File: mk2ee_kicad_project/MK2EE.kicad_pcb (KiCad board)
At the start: 2 copper layers, 209.5 x 132.1 mm, 81 parts, among them J1 L712RA, J10 Conn_01x02_Male, J11 Conn_02x6_Male, J12 Conn_01x06_Male, J13 Conn_01x06_Male, J2 Conn_02x6_Male, J3 Conn_01x02_Male, J4 Conn_02x03_Male, J5 Conn_02x03_Male, J6 Conn_01x04_Male, J7 Conn_01x04_Male, J8 Conn_02x03_Male, J9 Conn_02x03_Male, U1 NUCLEO-F411RE, U10 AS5047D-ATSM, U11 74HC595, U2 TSR_1-24150, U3 NCP718xSN330, U4 TSR_1-2465, U5 NCP718xSN330, U6 74HC595, U7 DRV8818PWP, U8 AS5047D-ATSM, U9 74HC595

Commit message: PCB designs are updated
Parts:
- added H5: MountingHole_3.2mm_M3, MountingHole:MountingHole_3.2mm_M3, F.Cu at (136.3, 148.4)
- added H5: MountingHole_3.2mm_M3, MountingHole:MountingHole_3.2mm_M3, F.Cu at (167.3, 179.4)
- C10, C11, C12, C13, C6, C7, C9, J7, R1, R6, R7, R8, U4, U7: moved to B.Cu
- R2, R3, R4, R5: footprint Resistor_SMD:R_0805_2012Metric_Pad1.15x1.40mm_HandSolder -> Resistor_SMD:R_1206_3216Metric; moved to B.Cu
- moved C6 224.8 mm to (246.9, 116.6), turned to 270 degrees
- moved C7 214.1 mm to (246.0, 132.7), turned to 90 degrees
- moved R1 199.5 mm to (249.4, 116.6), turned to 270 degrees
- moved R6 181.8 mm to (248.4, 132.7), turned to 90 degrees
- moved C13 179.4 mm to (247.5, 127.7)
- moved R3 176.1 mm to (247.5, 125.4), turned to 180 degrees
- moved R2 170.4 mm to (247.5, 123.0)
- moved U7 169.9 mm to (229.1, 127.9), turned to 180 degrees
- moved R5 166.8 mm to (246.7, 138.5), turned to 180 degrees
- moved R8 164.8 mm to (237.7, 136.7)
- moved R4 161.6 mm to (246.6, 140.9)
- moved R7 153.8 mm to (238.4, 116.2), turned to 90 degrees
- moved C10 153.7 mm to (213.9, 134.7), turned to 180 degrees
- moved C9 152.4 mm to (217.3, 125.2), turned to 90 degrees
- moved U6 151.7 mm to (229.2, 140.1), turned to 270 degrees
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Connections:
- R2 pad 2: VCC2 -> VCCB3v3
- R4 pad 2: VCC2 -> VCCB3v3
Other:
- board size 209.5 x 132.1 mm -> 163.6 x 169.7 mm

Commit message: all components are connected
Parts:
- added REF**: MountingHole_3.2mm_M3, MountingHole:MountingHole_3.2mm_M3, F.Cu at (163.1, 68.9)
- added REF**: MountingHole_3.2mm_M3, MountingHole:MountingHole_3.2mm_M3, F.Cu at (163.1, 47.9)
- C11: moved to F.Cu
- C19, C8, J10, J8, J9: moved to B.Cu
- J11, J2: footprint Connector_PinSocket_2.54mm:PinSocket_2x06_P2.54mm_Horizontal -> Connector_IDC:IDC-Header_2x06_P2.54mm_Horizontal
- TP1, TP2, TP3, TP4, TP5, TP7, TP8, TP9: footprint TestPoint:TestPoint_Pad_D4.0mm -> TestPoint:TestPoint_Pad_D1.5mm
- moved LED2 94.7 mm to (149.2, 89.7)
- moved C6 91.4 mm to (162.5, 151.6), turned to 0 degrees
- moved R7 90.1 mm to (153.6, 146.6), turned to 180 degrees
- moved C13 89.7 mm to (160.3, 148.6)
- moved R3 89.7 mm to (160.3, 146.3)
- moved R2 89.6 mm to (160.3, 143.9)
- moved R1 89.2 mm to (167.4, 151.6), turned to 180 degrees
- moved C7 86.6 mm to (162.5, 155.2), turned to 0 degrees
- moved R14 86.1 mm to (153.0, 85.4), turned to 270 degrees
- moved R8 84.2 mm to (156.9, 160.3), turned to 270 degrees
- moved R6 84.1 mm to (167.4, 155.2), turned to 180 degrees
- moved C9 82.8 mm to (140.3, 155.6), turned to 180 degrees
- moved U6 82.3 mm to (151.1, 166.2)
- moved U7 82.3 mm to (151.1, 154.0)
- moved R12 79.5 mm to (149.3, 85.4), turned to 90 degrees
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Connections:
- J11 pad 10: SerialDataDr4 -> SerialDataInEn4
- J11 pad 11: PO-CLKDr4 -> CLKEn4
- J11 pad 12: SH-CLKDr4 -> PO-CLKDr4
- J11 pad 2: GND -> VCCF3v3
- J11 pad 3: VCCF3v3 -> GND
- J11 pad 4: PWM4 -> SH-CLKEn4
- J11 pad 5: CLKEn4 -> SerialDataDr4
- J11 pad 6: MISO4 -> PO-CLKEn4
- J11 pad 7: SerialDataInEn4 -> SH-CLKDr4
- J11 pad 8: PO-CLKEn4 -> MISO4
- J11 pad 9: SH-CLKEn4 -> PWM4
- J12 pad 1: PO-CLKEn4 -> VMC
- J12 pad 2: SerialDataOutEn4 -> GND
- J12 pad 3: CLKEn4 -> Net-(J12-Pad3)
- J12 pad 4: MISO4 -> SerialDataDr4
- J12 pad 5: SH-CLKEn4 -> MISO4
- J12 pad 6: Net-(J12-Pad6) -> CLKEn4
- J13 pad 1: GND -> PO-CLKEn4
- J13 pad 2: VMC -> SH-CLKEn4
- J13 pad 3: SerialDataDr4 -> SerialDataOutEn4
- J13 pad 4: PO-CLKDr4 -> SH-CLKDr4
- J13 pad 5: SH-CLKDr4 -> PWM4
- J13 pad 6: PWM4 -> PO-CLKDr4
- J2 pad 1: VMA -> CLK1
- J2 pad 10: SerialDataOutDr1 -> SH-CLKEn1
- J2 pad 11: PO-CLKDr1 -> VMA
- J2 pad 12: SH-CLKDr1 -> VCCA3v3
- J2 pad 2: GND -> PO-CLKDr1
- J2 pad 3: VCCA3v3 -> PWM1
- J2 pad 4: PWM1 -> SerialDataOutEn1
- J2 pad 5: MOSI1 -> SH-CLKDr1
- J2 pad 7: SerialDataOutEn1 -> SerialDataOutDr1
- J2 pad 9: SH-CLKEn1 -> GND
- J4 pad 1: VMB -> SerialDataInDr2
- J4 pad 2: GND -> VMB
- J4 pad 4: SerialDataInDr2 -> PWM2
- J4 pad 5: PWM2 -> SH-CLKDr2
- J4 pad 6: SH-CLKDr2 -> GND
- J5 pad 1: VMB -> SH-CLKDr2
- J5 pad 4: SerialDataOutDr2 -> PWM2
- J5 pad 5: PWM2 -> SerialDataOutDr2
- J5 pad 6: SH-CLKDr2 -> VMB
- J6 pad 2: GND -> PWM2
- J6 pad 3: PWM2 -> VCC6v5
- J6 pad 4: VCC6v5 -> GND
- J8 pad 1: PO-CLKEn3 -> SerialDataInEn3
- J8 pad 2: SerialDataInEn3 -> Net-(J8-Pad2)
- J8 pad 3: CLKEn3 -> PO-CLKEn3
- J8 pad 4: MISO3 -> CLKEn3
- J8 pad 6: Net-(J8-Pad6) -> MISO3
- J9 pad 1: PO-CLKEn3 -> SH-CLKEn3
- J9 pad 2: SerialDataOutEn3 -> MISO3
- J9 pad 3: CLKEn3 -> PO-CLKEn3
- J9 pad 4: MISO3 -> CLKEn3
- J9 pad 5: SH-CLKEn3 -> SerialDataOutEn3
- U1 pad CN10_16: Net-(U1-PadCN10_16) -> PO-CLKEn1
- U1 pad CN10_24: PO-CLKEn1 -> Net-(U1-PadCN10_24)
- U1 pad CN10_30: Net-(U1-PadCN10_30) -> SH-CLKEn1
- U1 pad CN10_33: MOSI1 -> Net-(U1-PadCN10_33)
- U1 pad CN7_34: SH-CLKEn1 -> CLK1
- U6 pad 1: USM0 -> USM1
- U6 pad 2: USM1 -> USM0
- U6 pad 3: STEP -> SRn
- U6 pad 4: SRn -> RESETn
- U6 pad 5: RESETn -> STEP
- U9 pad 15: CSn3 -> Net-(U9-Pad15)
- U9 pad 4: LED2-R3 -> LED2-B3
- U9 pad 6: LED2-B3 -> LED2-R3
- U9 pad 7: Net-(U9-Pad7) -> CSn3
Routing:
- net VMB: track 0.00 -> 175.0 mm, vias 0 -> 4
- net VMA: track 0.00 -> 133.7 mm
- net GND: track 0.00 -> 118.1 mm, vias 0 -> 16
- net PWM2: track 0.00 -> 103.1 mm
- net MISO3: track 0.00 -> 91.0 mm, vias 0 -> 1
- net CLKEn3: track 0.00 -> 83.8 mm, vias 0 -> 1
- net PO-CLKEn3: track 0.00 -> 61.0 mm
- net SH-CLKEn3: track 0.00 -> 59.0 mm
- net VCCA3v3: track 0.00 -> 55.6 mm
- net VCCA5V: track 0.00 -> 55.4 mm
- net MISO4: track 0.00 -> 55.2 mm
- net PO-CLKEn4: track 0.00 -> 55.1 mm, vias 0 -> 1
- net PWM4: track 0.00 -> 54.9 mm
- net CLKEn4: track 0.00 -> 53.8 mm, vias 0 -> 1
- net MISO1: track 0.00 -> 51.0 mm
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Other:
- board size 163.6 x 169.7 mm -> 173.3 x 172.9 mm

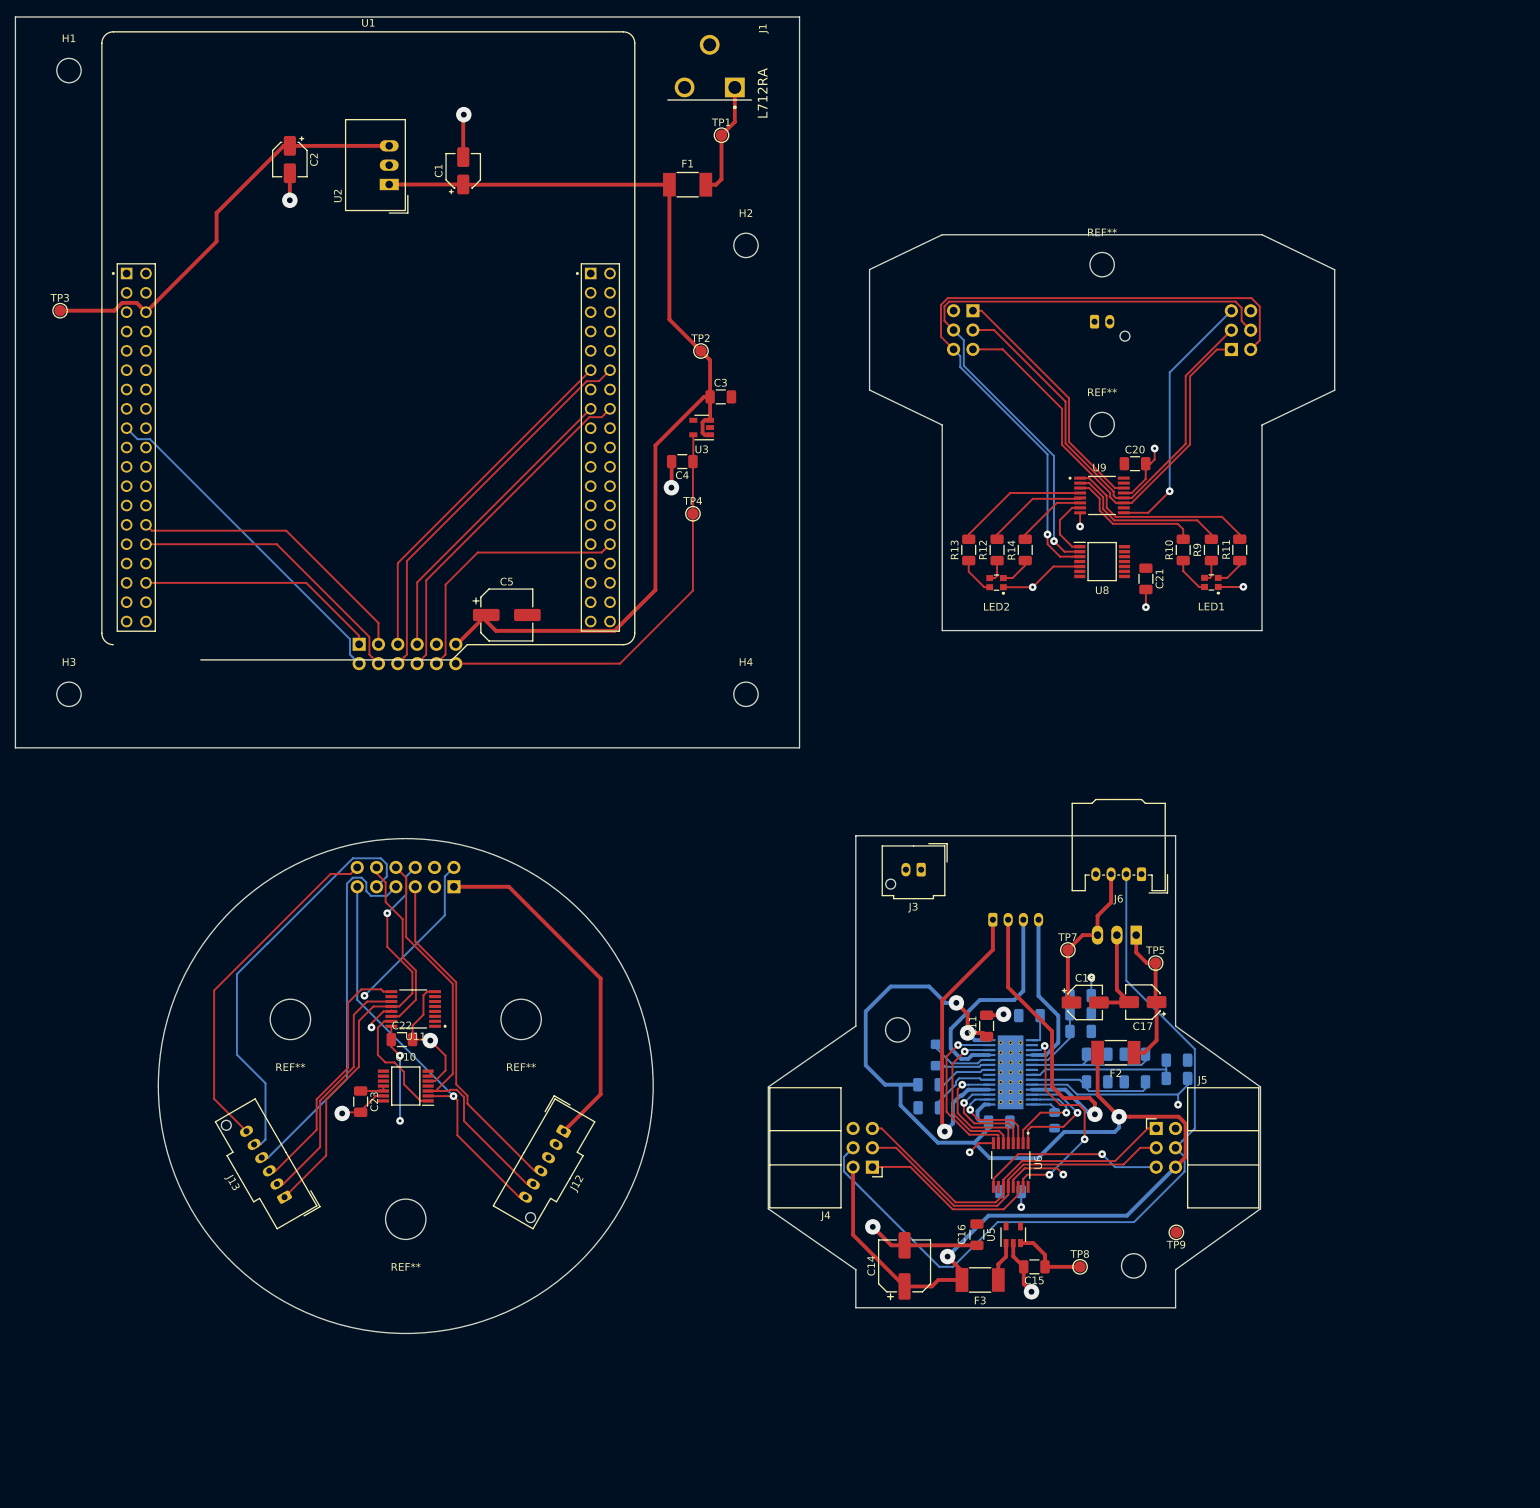
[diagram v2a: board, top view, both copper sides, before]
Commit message: New 3D model of Base part and PCB design is fixed
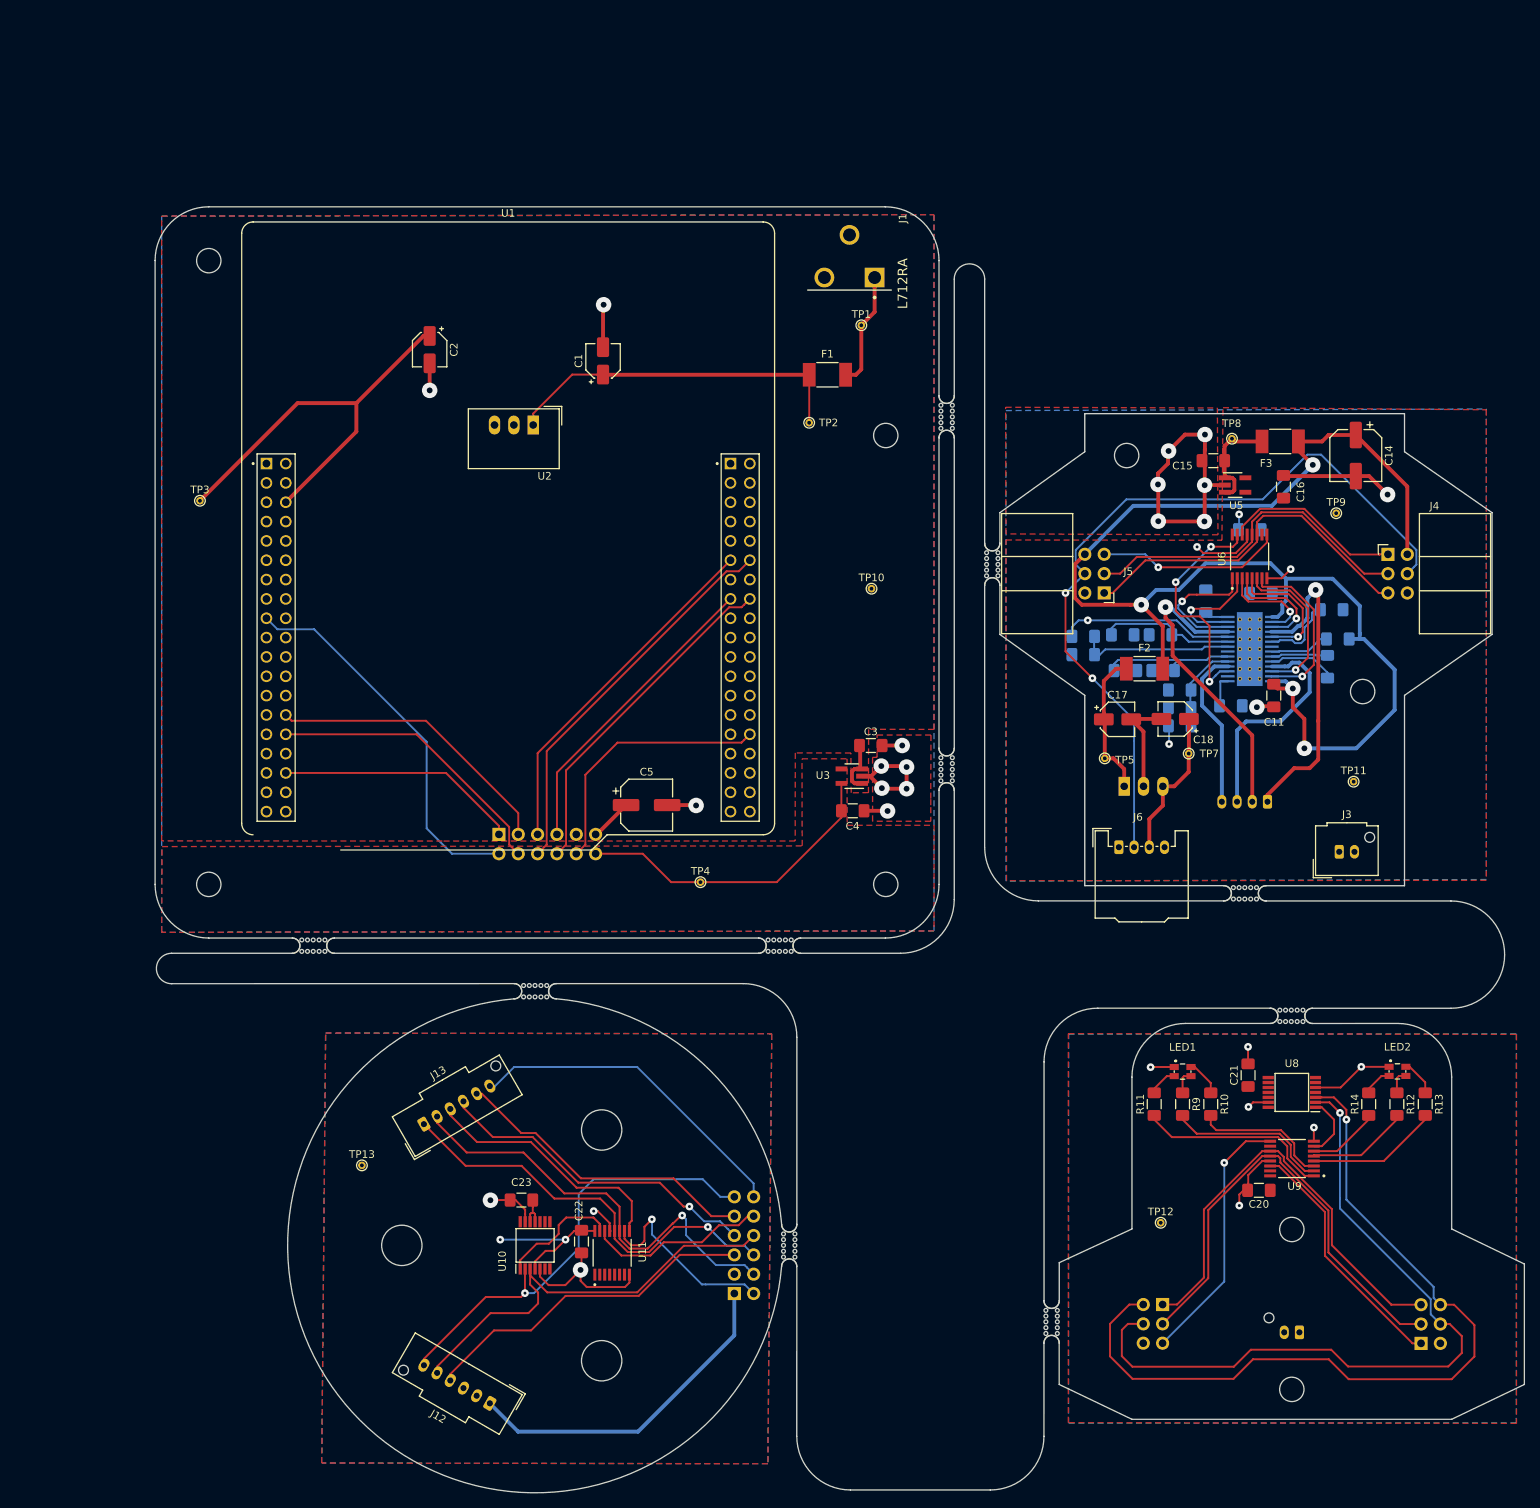
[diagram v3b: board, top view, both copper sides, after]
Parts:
- removed the H5 at (136.3, 148.4)
- removed the H5 at (167.3, 179.4)
- removed the REF** at (163.1, 68.9)
- removed the REF** at (163.1, 47.9)
- added H5: MountingHole_3.2mm_M3, MountingHole:MountingHole_3.2mm_M3, F.Cu at (197.3, 104.0)
- added H5: MountingHole_3.2mm_M3, MountingHole:MountingHole_3.2mm_M3, F.Cu at (166.3, 73.0)
- added REF**: MountingHole_3.2mm_M3, MountingHole:MountingHole_3.2mm_M3, F.Cu at (188.0, 174.6)
- added REF**: MountingHole_3.2mm_M3, MountingHole:MountingHole_3.2mm_M3, F.Cu at (188.0, 195.6)
- added TP10: GND, TestPoint:TestPoint_THTPad_D1.0mm_Drill0.5mm, F.Cu at (132.8, 90.5)
- added TP11: TestPoint, TestPoint:TestPoint_THTPad_D1.0mm_Drill0.5mm, F.Cu at (196.2, 115.8)
- added TP12: TestPoint, TestPoint:TestPoint_THTPad_D1.0mm_Drill0.5mm, F.Cu at (170.8, 173.8)
- added TP13: TestPoint, TestPoint:TestPoint_THTPad_D1.0mm_Drill0.5mm, F.Cu at (65.9, 166.2)
- added mouse-bite-3mm-slot: VAL**, MK2Library:mouse-bite-3mm-slot, F.Cu at (148.7, 87.3)
- added mouse-bite-3mm-slot: VAL**, MK2Library:mouse-bite-3mm-slot, F.Cu at (88.6, 143.3)
- added mouse-bite-3mm-slot: VAL**, MK2Library:mouse-bite-3mm-slot, F.Cu at (142.7, 67.9)
- added mouse-bite-3mm-slot: VAL**, MK2Library:mouse-bite-3mm-slot, F.Cu at (142.7, 114.2)
- added mouse-bite-3mm-slot: VAL**, MK2Library:mouse-bite-3mm-slot, F.Cu at (181.9, 130.5)
- added mouse-bite-3mm-slot: VAL**, MK2Library:mouse-bite-3mm-slot, F.Cu at (188.0, 146.6)
- added mouse-bite-3mm-slot: VAL**, MK2Library:mouse-bite-3mm-slot, F.Cu at (156.5, 186.8)
- added mouse-bite-3mm-slot: VAL**, MK2Library:mouse-bite-3mm-slot, F.Cu at (120.8, 137.4)
- added mouse-bite-3mm-slot: VAL**, MK2Library:mouse-bite-3mm-slot, F.Cu at (59.5, 137.4)
- added mouse-bite-3mm-slot: VAL**, MK2Library:mouse-bite-3mm-slot, F.Cu at (122.0, 176.7)
- C10, C11, C12, C13, C15, C16, C19, C20, C21, C22, C23, C3, C4, C6, C7, C8, C9: footprint Capacitor_SMD:C_1206_3216Metric -> Capacitor_SMD:C_1206_3216Metric_Pad1.42x1.75mm_HandSolder
- R1, R10, R11, R12, R13, R14, R2, R3, R4, R5, R6, R7, R9: footprint Resistor_SMD:R_1206_3216Metric -> Resistor_SMD:R_1206_3216Metric_Pad1.42x1.75mm_HandSolder
- R8: footprint Resistor_SMD:R_0805_2012Metric_Pad1.15x1.40mm_HandSolder -> Resistor_SMD:R_1206_3216Metric_Pad1.42x1.75mm_HandSolder
- TP1, TP2, TP3, TP4, TP5, TP7, TP8, TP9: footprint TestPoint:TestPoint_Pad_D1.5mm -> TestPoint:TestPoint_THTPad_D1.0mm_Drill0.5mm
- U3, U5: footprint Package_TO_SOT_SMD:SOT-23-5 -> Package_TO_SOT_SMD:SOT-23-5_HandSoldering
- moved J8 147.9 mm to (205.0, 189.6), turned to 0 degrees
- moved J10 135.5 mm to (189.0, 188.2), turned to 180 degrees
- moved J9 125.8 mm to (171.1, 184.5), turned to 180 degrees
- moved C14 121.8 mm to (196.4, 73.0), turned to 270 degrees
- moved F3 117.0 mm to (186.5, 71.1), turned to 180 degrees
- moved TP8 110.6 mm to (180.2, 70.8), turned to 180 degrees
- moved C15 108.5 mm to (177.7, 73.7)
- moved C16 106.2 mm to (186.9, 77.1), turned to 90 degrees
- moved J4 105.2 mm to (200.7, 86.0), turned to 0 degrees
- moved U5 102.7 mm to (180.6, 76.9), turned to 0 degrees
- moved C20 96.8 mm to (183.7, 169.5), turned to 180 degrees
- moved TP9 96.8 mm to (193.9, 80.6), turned to 0 degrees
- moved R13 94.3 mm to (205.6, 158.2), turned to 270 degrees
- moved C19 92.4 mm to (182.5, 82.7), turned to 0 degrees
- moved U9 90.6 mm to (188.1, 165.3), turned to 180 degrees
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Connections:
- C1 pad 1: VMA -> /supply/pwr2
- C3 pad 1: VMA -> VCCA5V
- C5 pad 1: VMA -> VCCA5V
- F1 pad P$2: VMA -> /supply/pwr2
- J2 pad 11: VMA -> VCCA5V
- TP2 pad 1: VMA -> /supply/pwr2
- U2 pad 1: VMA -> /supply/pwr2
- U3 pad 1: VMA -> VCCA5V
- U3 pad 3: VMA -> VCCA5V
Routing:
- net VMA: track 133.7 -> 0.00 mm
- net GND: track 118.1 -> 172.9 mm, vias 16 -> 28
- net /supply/pwr2: track 0.00 -> 46.2 mm
- net SH-CLKEn4: track 32.5 -> 57.9 mm, vias 0 -> 1
- net MISO3: track 91.0 -> 107.5 mm
- net PWM4: track 54.9 -> 40.5 mm
- net VCCA3v3: track 55.6 -> 41.8 mm
- net CLKEn3: track 83.8 -> 97.3 mm
- net VCCA5V: track 55.4 -> 68.8 mm
- net VCCF3v3: track 38.3 -> 49.6 mm
- net CLKEn4: track 53.8 -> 59.9 mm
- net SH-CLKDr4: track 50.0 -> 44.2 mm, vias 0 -> 1
- net PO-CLKDr1: track 44.5 -> 50.0 mm
- net /driver-1/2A: track 41.9 -> 39.9 mm
- net VMB: track 175.0 -> 177.0 mm
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- added copper zone on B.Cu, net GND
- added copper zone on F.Cu, net GND
- added copper zone on F.Cu, net VCCA3v3
- added copper zone on F.Cu, net VCCA5V
- added copper zone on F.Cu, net VCCB3v3
- added copper zone on F.Cu, net VCCD3v3
- added copper zone on F.Cu, net VCCF3v3
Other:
- board size 173.3 x 172.9 mm -> 179.9 x 168.9 mm
- net class Default: clearance 0.2032 -> 0.1
- rule trace_clearance: 0.2032 -> 0.1
- rule trace_min: 0.2032 -> 0.254
